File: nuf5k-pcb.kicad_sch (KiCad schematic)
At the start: 226 parts, among them J1 AVR-ISP-6, J2 1734366-1, J3 1734366-1, J4 1734366-1, SW0 KEYSW, SW1 KEYSW, SW10 KEYSW, SW11 KEYSW, SW12 KEYSW, SW13 KEYSW, SW14 KEYSW, SW15 KEYSW, SW16 KEYSW, SW17 KEYSW, SW18 KEYSW, SW19 KEYSW, SW2 KEYSW, SW20 KEYSW, SW21 KEYSW, SW22 KEYSW, SW23 KEYSW, SW24 KEYSW, SW25 KEYSW, SW26 KEYSW, SW27 KEYSW, SW28 KEYSW, SW29 KEYSW, SW3 KEYSW, SW30 KEYSW, SW31 KEYSW, SW32 KEYSW, SW33 KEYSW, SW34 KEYSW, SW35 KEYSW, SW36 KEYSW, SW37 KEYSW, SW38 KEYSW, SW39 KEYSW, SW4 KEYSW, SW40 KEYSW, SW41 KEYSW, SW42 KEYSW, SW43 KEYSW, SW44 KEYSW, SW45 KEYSW, SW46 KEYSW, SW47 KEYSW, SW48 KEYSW, SW49 KEYSW, SW5 KEYSW, SW50 KEYSW, SW51 KEYSW, SW52 KEYSW, SW53 KEYSW, SW54 KEYSW, SW55 KEYSW, SW56 KEYSW, SW57 KEYSW, SW58 KEYSW, SW59 KEYSW, SW6 KEYSW, SW60 KEYSW, SW61 KEYSW, SW62 KEYSW, SW63 KEYSW, SW64 KEYSW, SW65 KEYSW, SW66 KEYSW, SW67 KEYSW, SW68 KEYSW, SW69 KEYSW, SW7 KEYSW, SW70 KEYSW, SW71 KEYSW, SW72 KEYSW, SW73 KEYSW, SW74 KEYSW, SW75 KEYSW, SW76 KEYSW, SW77 KEYSW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

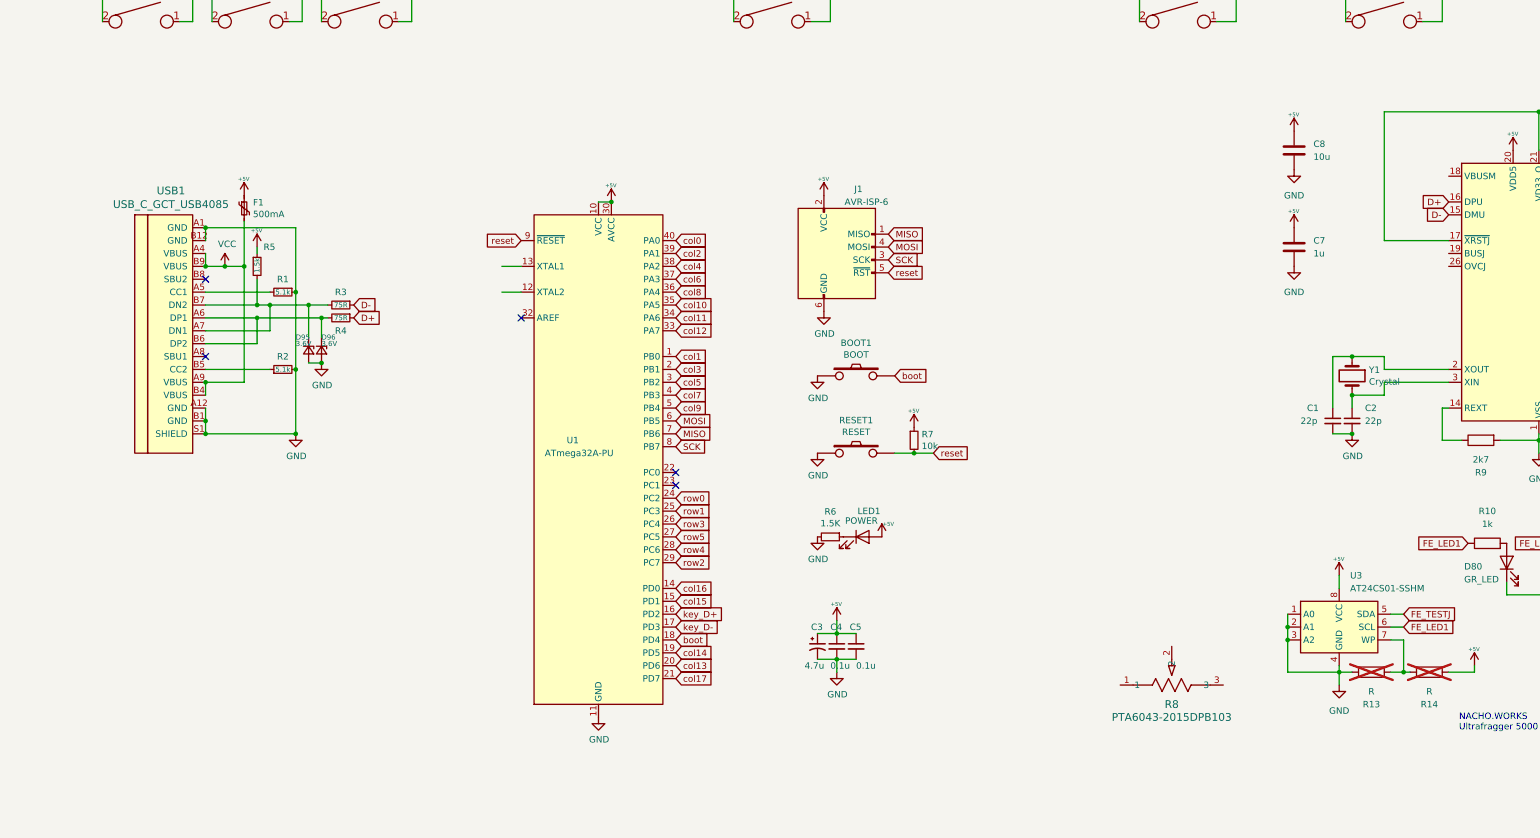
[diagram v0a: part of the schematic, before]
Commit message: added volume button
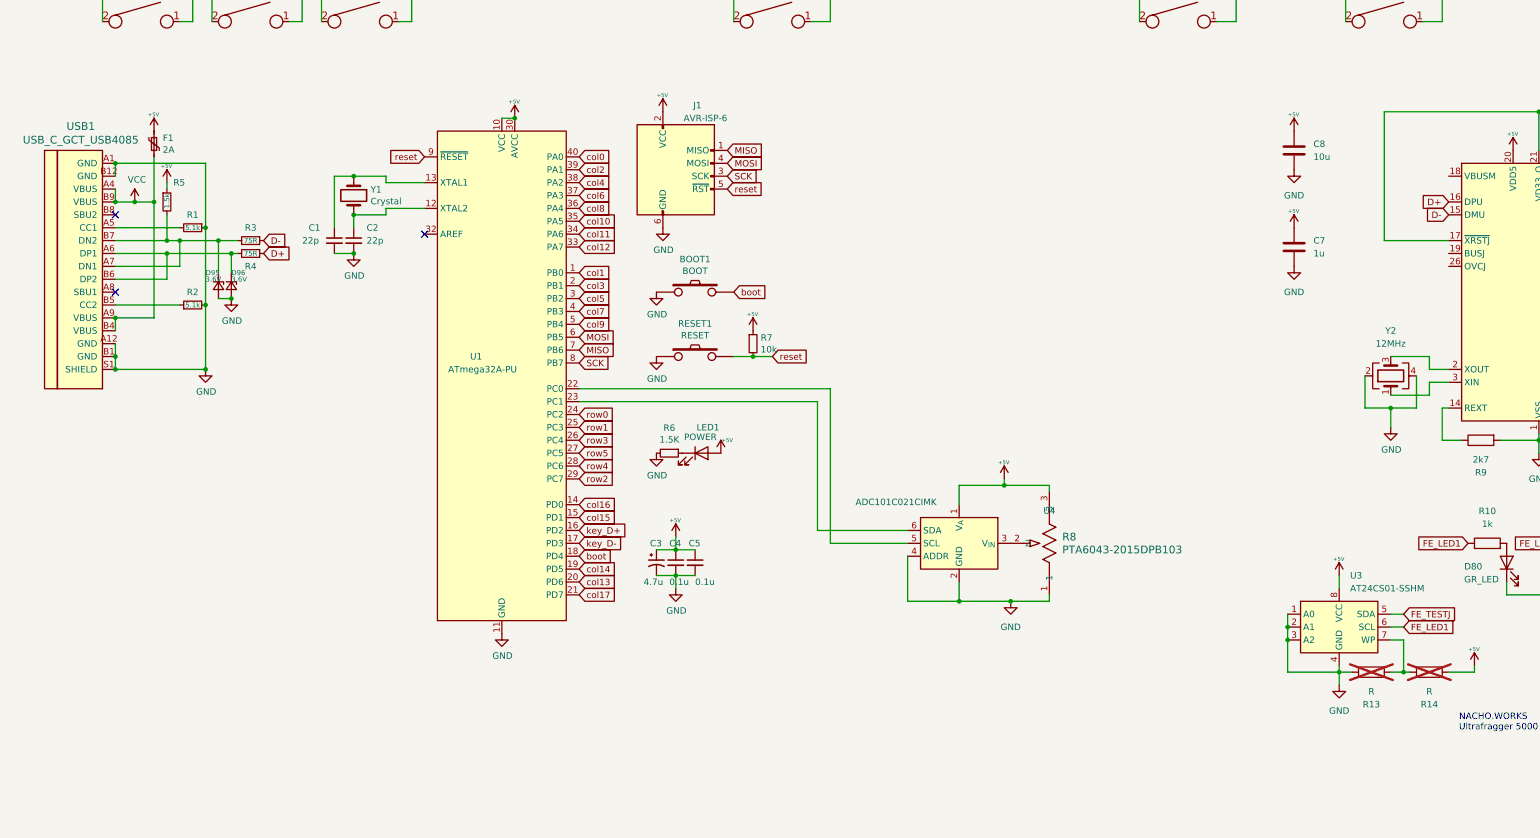
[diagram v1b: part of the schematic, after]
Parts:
- added U4: ADC101C021CIMK, Package_TO_SOT_SMD:SOT-23-6, symbol Analog_ADC:ADC101C021CIMK
- added Y2: 12MHz, Crystal:Crystal_SMD_3225-4Pin_3.2x2.5mm, symbol Device:Crystal_GND24
- F1: value 500mA -> 2A
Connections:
- net +5V: now also R8.3, U4.1 (V_{A})
- net GND: now also R8.1, U4.2 (GND), U4.4 (ADDR), Y2.2, Y2.4
- net at U1.12 (XTAL2): now also C2.1, Y1.2
- net at U1.13 (XTAL1): now also C1.1, Y1.1
- net at U1.22 (PC0): now also U4.5 (SCL)
- net at U1.23 (PC1): now also U4.6 (SDA)
- net at R8.2: now also U4.3 (V_{IN})
- new net: U2.2 (XOUT), Y2.3
- new net: U2.3 (XIN), Y2.1
- no-connect marks 5 -> 3
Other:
- moved on the sheet: BOOT1, C1, C2, C3, C4, C5, D95, D96, F1, J1, LED1, R1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
